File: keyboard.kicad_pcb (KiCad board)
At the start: 2 copper layers, 69.1 x 68.1 mm, 78 parts, among them CON1 USB-MICRO-B, J1 CONN-PALM-FOLD-KB, P1 Keyboard Even, P2 Keyboard Odd, P3 PS2, P4 Palm Serial, P5 ARM debug header, P6 Power, P7 USB_H, Q1 BSS138, Q2 BSS138, Q3 BSS138, SW1 SW_PUSH, U1 CONN-X220-KB, U2 MCP1700-2202E/TT, U3 EFM32G222F32, X1 CRYSTAL

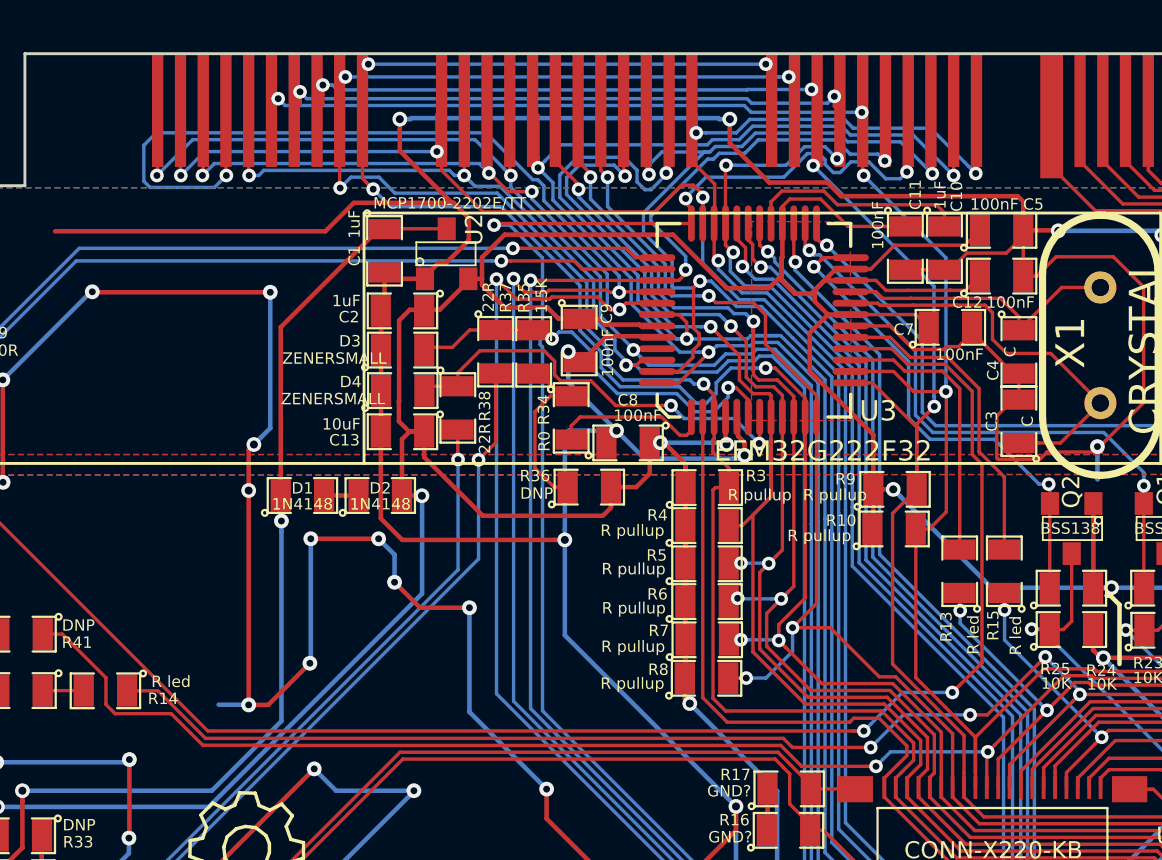
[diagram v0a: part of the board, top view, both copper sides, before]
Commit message: Imported board_redraw_dimensions.dxf and adjusted the Palm footprint to match.  Note: it still needs fixing in module
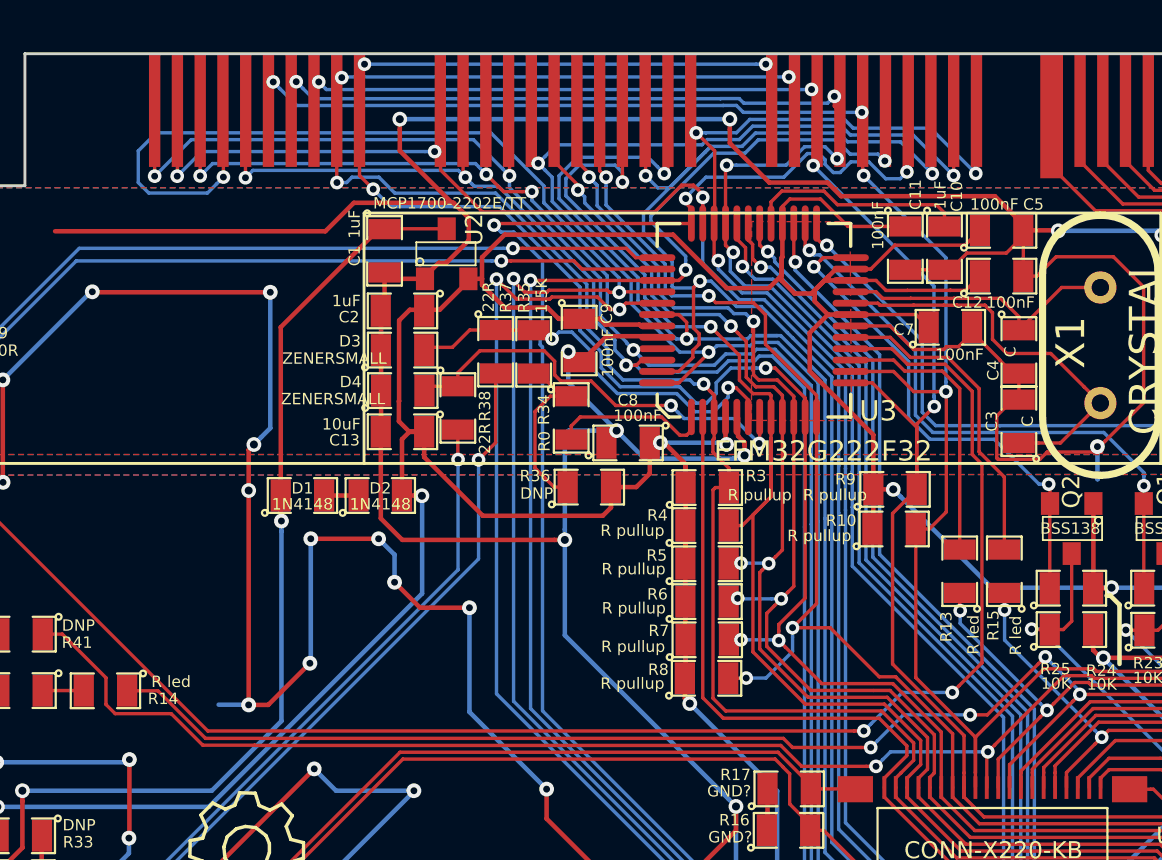
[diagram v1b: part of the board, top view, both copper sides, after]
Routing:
- net col8: track 115.0 -> 112.6 mm
- net row8: track 144.5 -> 145.8 mm
- net col1: track 95.1 -> 94.0 mm
- net col4: track 98.6 -> 97.8 mm
- net row1: track 122.1 -> 122.8 mm
- net col12: track 106.4 -> 107.2 mm
- net GND: track 578.5 -> 577.9 mm
- net col6: track 115.3 -> 115.9 mm
- net col3: track 114.8 -> 115.4 mm
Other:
- board text added: "0.55"
- board text added: "18"
- board text added: "5.45"
- board text added: "69.1"
- board text added: "J1"
- board text added: "J2"
- board text added: "J3"
- board text added: "J4"

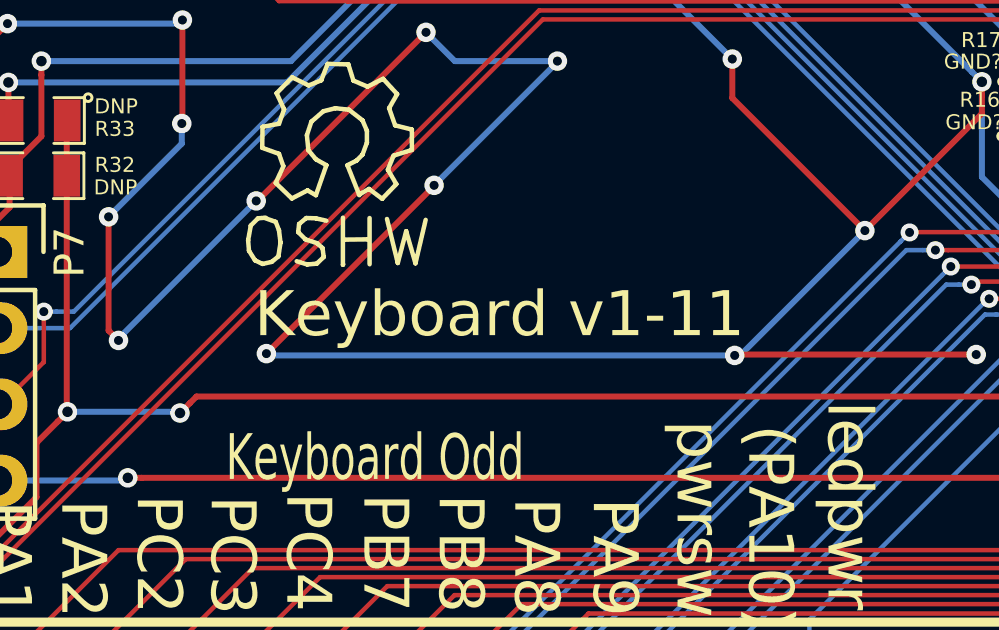
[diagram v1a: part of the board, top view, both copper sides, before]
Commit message: Bump version number on silkscreen
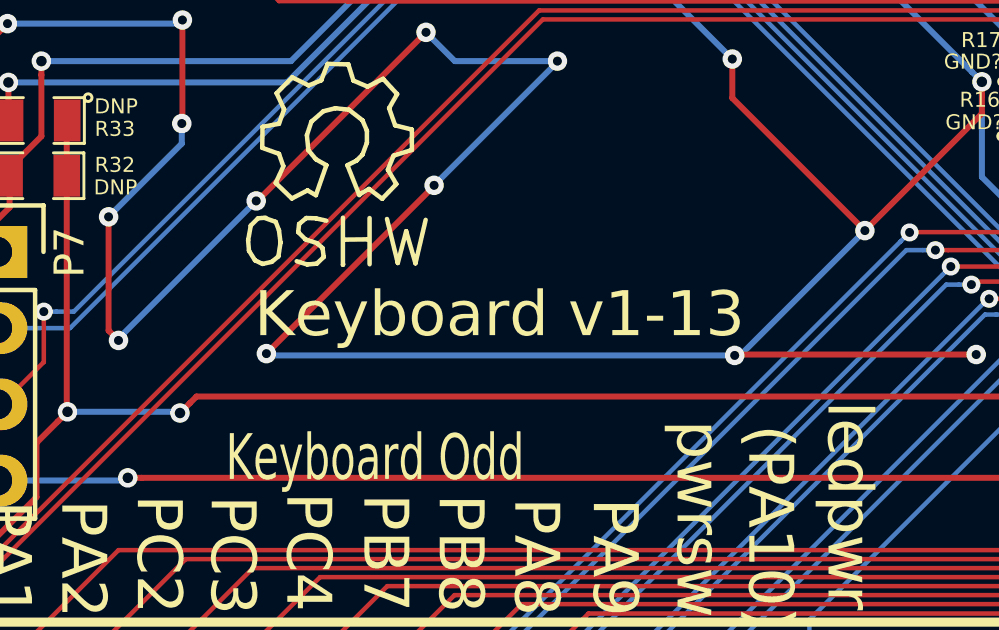
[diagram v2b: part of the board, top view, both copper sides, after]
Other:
- board text added: "Keyboard v1-13"
- board text removed: "Keyboard v1-11"

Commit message: Do DRC and reflow fill
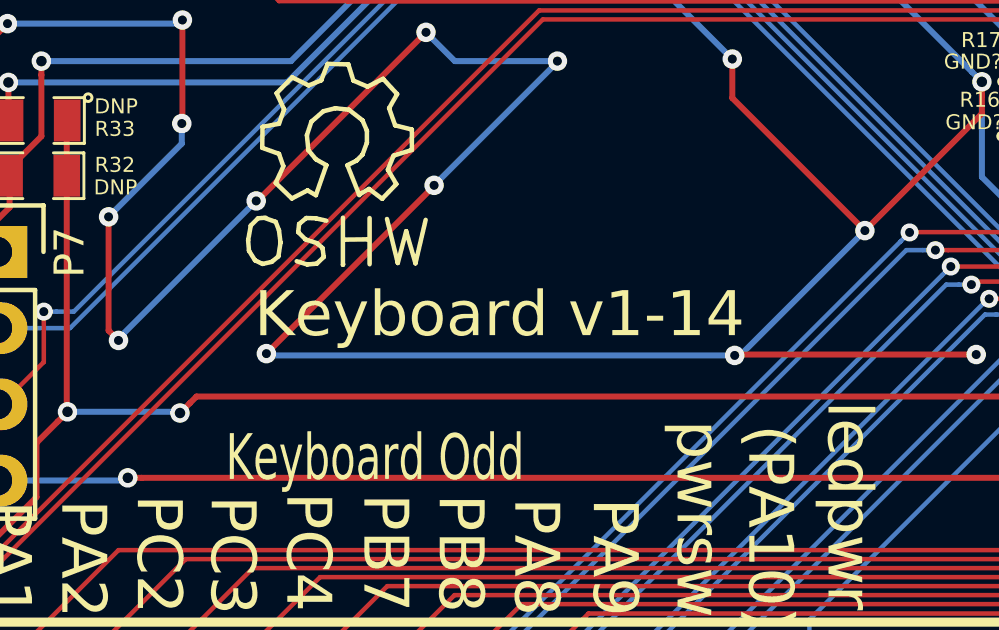
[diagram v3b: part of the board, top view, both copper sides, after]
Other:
- board text added: "Keyboard v1-14"
- board text removed: "Keyboard v1-13"

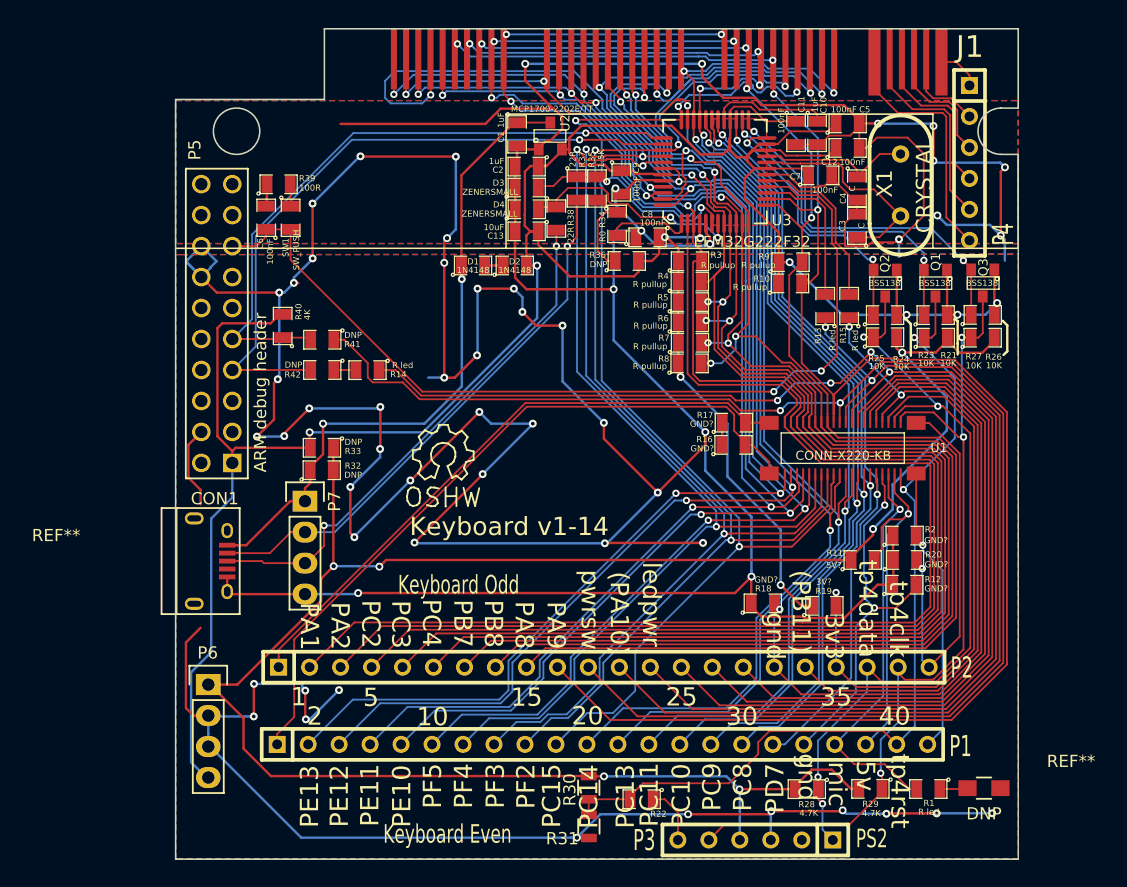
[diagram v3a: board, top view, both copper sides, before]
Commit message: Clean up silkscreen cheat sheet, mostly moving breakout description
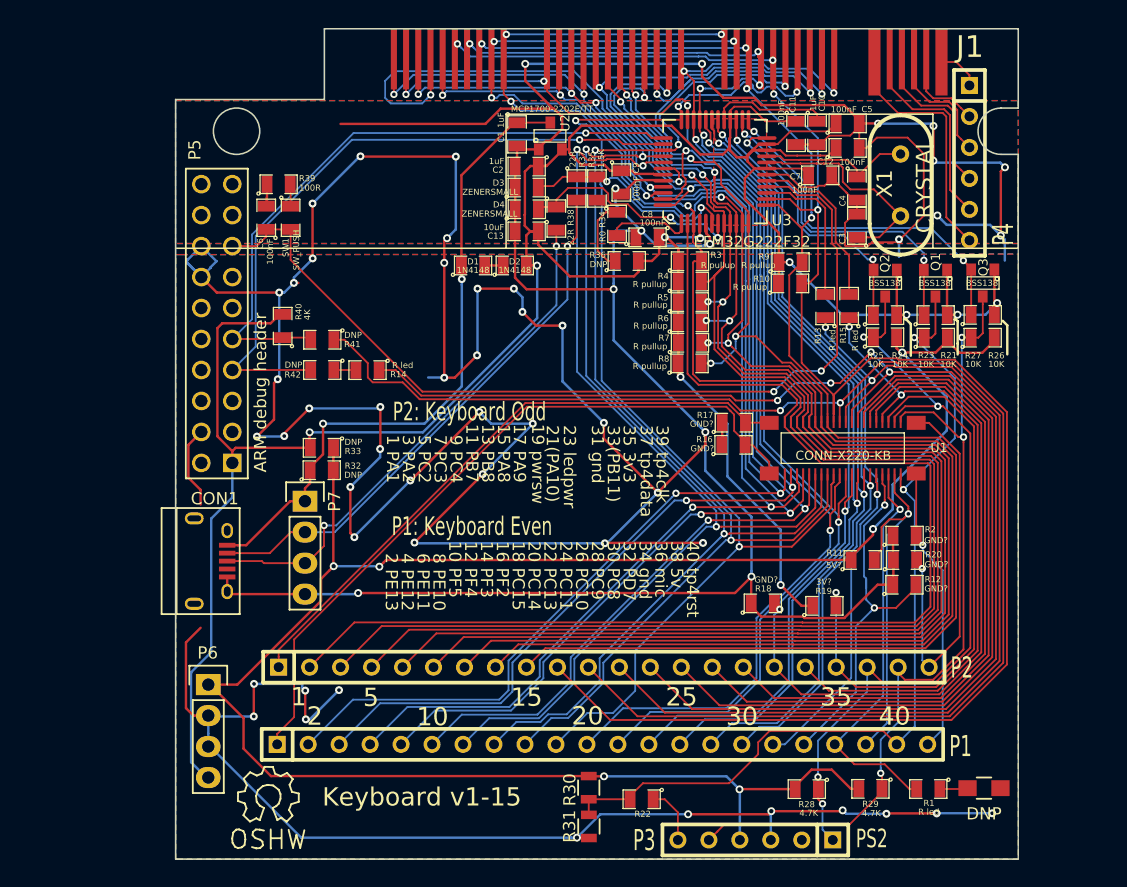
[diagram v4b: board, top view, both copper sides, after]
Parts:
- P1: value Keyboard Even -> P1: Keyboard Even
- P2: value Keyboard Odd -> P2: Keyboard Odd
- moved REF** 31.5 mm to (137.6, 106.0)
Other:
- board text added: "1 PA1"
- board text added: "10 PF5"
- board text added: "11 PB7"
- board text added: "12 PF4"
- board text added: "13 PB8"
- board text added: "14 PF3"
- board text added: "15 PA8"
- board text added: "16 PF2"
- board text added: "17 PA9"
- board text added: "18 PC15"
- board text added: "19 pwrsw"
- board text added: "2 PE13"
- board text added: "20 PC14"
- board text added: "21(PA10)"
- board text added: "22 PC13"
- board text added: "23 ledpwr"
- board text added: "24 PC11"
- board text added: "26 PC10"
- board text added: "28 PC9"
- board text added: "3 PA2"
- board text added: "30 PC8"
- board text added: "31 gnd"
- board text added: "32 PD7"
- board text added: "33(PB11)"
- board text added: "34 gnd"
- board text added: "35 3v3"
- board text added: "36 mic"
- board text added: "37 tp4data"
- board text added: "38 5v"
- board text added: "39 tp4clk"
- board text added: "4 PE12"
- board text added: "40 tp4rst"
- board text added: "5 PC2"
- board text added: "6 PE11"
- board text added: "7 PC3"
- board text added: "8 PE10"
- board text added: "9 PC4"
- board text added: "Keyboard v1-15"
- board text removed: "(PA10)"
- board text removed: "(PB11)"
- board text removed: "3v3"
- board text removed: "5v"
- board text removed: "Keyboard v1-14"
- board text removed: "PA1"
- board text removed: "PA2"
- board text removed: "PA8"
- board text removed: "PA9"
- board text removed: "PB7"
- board text removed: "PB8"
- board text removed: "PC10"
- board text removed: "PC11"
- board text removed: "PC13"
- board text removed: "PC14"
- board text removed: "PC15"
- board text removed: "PC2"
- board text removed: "PC3"
- board text removed: "PC4"
- board text removed: "PC8"
- board text removed: "PC9"
- board text removed: "PD7"
- board text removed: "PE10"
- board text removed: "PE11"
- board text removed: "PE12"
- board text removed: "PE13"
- board text removed: "PF2"
- board text removed: "PF3"
- board text removed: "PF4"
- board text removed: "PF5"
- board text removed: "gnd"
- board text removed: "ledpwr"
- board text removed: "mic"
- board text removed: "pwrsw"
- board text removed: "tp4clk"
- board text removed: "tp4data"
- board text removed: "tp4rst"

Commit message: Increase size of x220 pad sizes
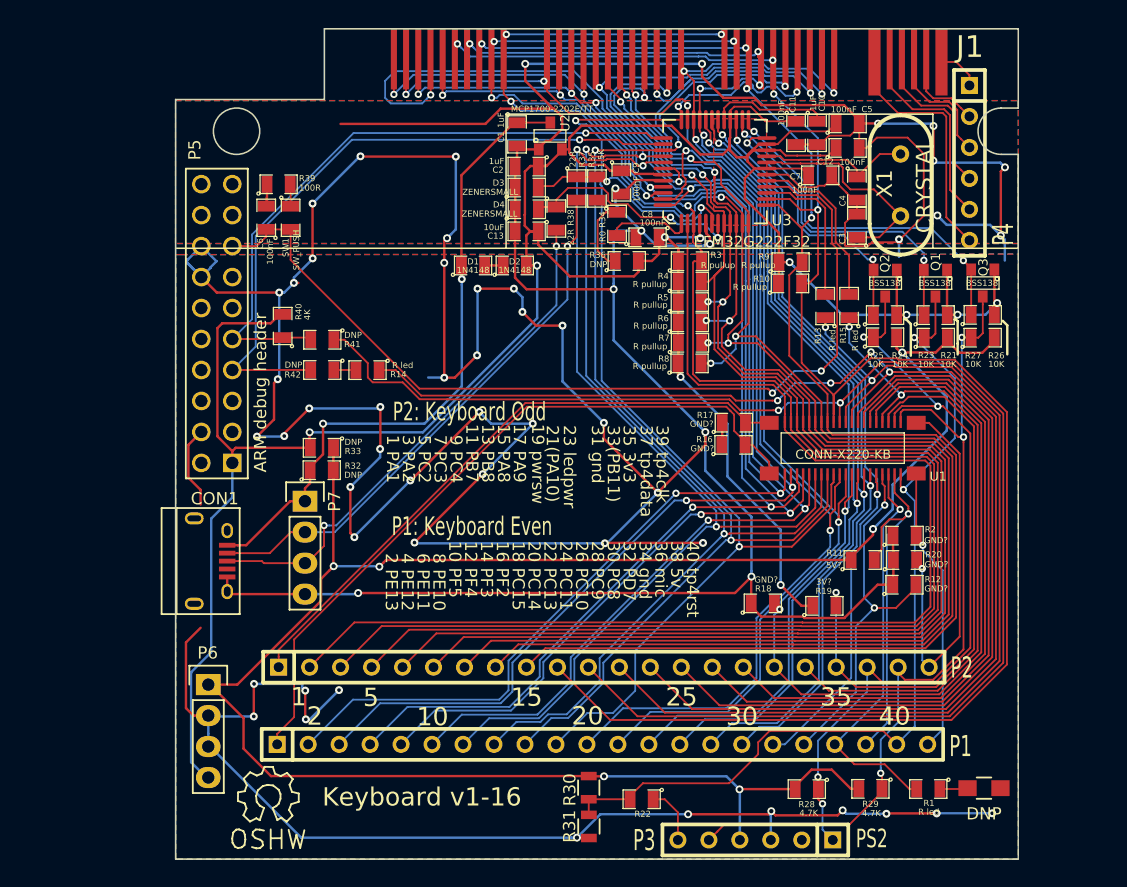
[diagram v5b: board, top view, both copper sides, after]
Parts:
- U1: footprint AA01B-S040VA1 -> AA01B-S040VA1:AA01B-S040VA1
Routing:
- net hotkey: track 102.6 -> 101.5 mm
- net row6: track 151.4 -> 150.5 mm
- net Net-(P1-Pad18): track 30.8 -> 30.0 mm
- net row1: track 122.8 -> 122.1 mm
- net row4: track 114.6 -> 114.0 mm
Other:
- board text added: "Keyboard v1-16"
- board text removed: "Keyboard v1-15"

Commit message: Add a project URL
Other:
- board text added: "Keyboard v1-18"
- board text added: "http://wob.zot.org/2/projects/show/keyboard"
- board text removed: "Keyboard v1-16"
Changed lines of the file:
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@@
     (area 88.101666 17.2128 214.297165 118.337754)
     (thickness 1.6)
-    (drawings 253)
+    (drawings 254)
     (tracks 2347)
     (zones 0)
@@
       (net 62 "Net-(P1-Pad1)"))
   )
+  (gr_text http://wob.zot.org/2/projects/show/keyboard (at 165.28 106.72) (layer B.SilkS)
+    (effects (font (size 1.5 1.5) (thickness 0.3)) (justify mirror))
+  )
   (gr_line (start 199.07 42.9972) (end 208.340143 42.9972) (layer Dwgs.User) (width 0.1))
   (gr_line (start 207.340143 58.4972) (end 207.340143 45.4972) (layer Dwgs.User) (width 0.1))
@@
     (effects (font (size 1.5 1.5) (thickness 0.3)))
   )
-  (gr_text "Keyboard v1-16" (at 150.2 106) (layer F.SilkS)
+  (gr_text "Keyboard v1-18" (at 150.11 104.62) (layer F.SilkS)
     (effects (font (size 1.5 1.5) (thickness 0.3)))
   )
